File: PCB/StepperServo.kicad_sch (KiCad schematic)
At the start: 69 parts

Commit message: Clean
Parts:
- removed P1: (no value), symbol Connector_Generic:Conn_01x02
- removed P5: (no value), symbol StepperServo-rescue:Conn_01x02-Connector_Generic-BTTS57Bv2-rescue
- added P3: Conn_01x04, Connector_JST:JST_XH_B4B-XH-A_1x04_P2.50mm_Vertical, symbol StepperServo-rescue:Conn_01x04-Connector_Generic-BTTS57Bv2-rescue
- C1, C10: value (none) -> 100uF 35V VT; footprint (none) -> Capacitor_SMD:CP_Elec_6.3x7.7
- C11, C12, C13, C14, C16, C18, C2, C20, C21, C4, C5, C8: value (none) -> C; footprint (none) -> Capacitor_SMD:C_0603_1608Metric
- C15, C3: value (none) -> 0.22uF; footprint (none) -> Capacitor_SMD:C_0805_2012Metric
- C17, C6, C7, C9: value (none) -> C; footprint (none) -> Capacitor_SMD:C_0805_2012Metric
- C19: value (none) -> 100nF; footprint (none) -> Capacitor_SMD:C_0603_1608Metric
- D1, D4: value (none) -> LED; footprint (none) -> LED_SMD:LED_0603_1608Metric
- D2, D3, D5: value (none) -> D; footprint (none) -> Diode_SMD:D_2512_6332Metric
- H1, H2, H3, H4, H5, H6, H7, H8: value (none) -> MountingHole_Pad; footprint (none) -> MountingHole:MountingHole_2.7mm_M2.5_ISO14580_Pad_TopBottom
- L1: value (none) -> 22uH; footprint (none) -> Inductor_SMD:L_Wuerth_MAPI-4030
- Mode-K3, Next-K2, RES-K1, Valid-K4: value (none) -> SW_Push; footprint (none) -> Button_Switch_SMD:SW_SPST_TL3342
- P2: value (none) -> Conn_01x04; footprint (none) -> Connector_JST:JST_XH_B4B-XH-A_1x04_P2.50mm_Vertical
- P4: value (none) -> Conn_01x08; footprint (none) -> Connector_PinHeader_2.54mm:PinHeader_1x08_P2.54mm_Vertical
- R1, R2: value (none) -> 0.1R; footprint (none) -> Resistor_SMD:R_2512_6332Metric
- R10, R11, R13, R14, R16, R17, R21, R23, R7: value (none) -> ?R; footprint (none) -> Resistor_SMD:R_0603_1608Metric
- R18: value (none) -> 470; footprint (none) -> Resistor_SMD:R_0805_2012Metric
- R19: value (none) -> ?R; footprint (none) -> Resistor_SMD:R_1206_3216Metric
- R20, R93: value (none) -> 1kR; footprint (none) -> Resistor_SMD:R_0603_1608Metric
- R22: value (none) -> 10k; footprint (none) -> Resistor_SMD:R_0603_1608Metric
- R6: value (none) -> 1k; footprint (none) -> Resistor_SMD:R_0603_1608Metric
- U1: value (none) -> AOZ1282CI; footprint (none) -> Package_TO_SOT_SMD:SOT-23-6
- U2, U4: value (none) -> A4950E; footprint (none) -> Package_SO:SOIC-8-1EP_3.9x4.9mm_P1.27mm_EP2.41x3.3mm
- U5: value (none) -> TLE5012B; footprint (none) -> Package_SO:Infineon_PG-DSO-8-27_3.9x4.9mm_EP2.65x3mm
- U7: value (none) -> STM32F103CBTx; footprint (none) -> Package_QFP:LQFP-48_7x7mm_P0.5mm
- U8: value (none) -> LD1117S33CTR; footprint (none) -> Package_TO_SOT_SMD:SOT-223
- U9: value (none) -> PCA82C251; footprint (none) -> Package_SO:SO-8_3.9x4.9mm_P1.27mm
- Y1: value (none) -> Crystal; footprint (none) -> Crystal:Crystal_SMD_EuroQuartz_MT-4Pin_3.2x2.5mm_HandSoldering
- p7: value (none) -> Conn_01x08; footprint (none) -> Connector_PinSocket_2.54mm:PinSocket_1x07_P2.54mm_Vertical
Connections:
- net GND: now also P3.4 (Pin_4)
- net VMOT: now also P3.1 (Pin_1)
- net CAN_L: now reaches R19.1, U9.6 (CAN-)
- net CAN_H: now reaches R19.2, U9.7 (CAN+)
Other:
- note added: "10mA"
- note added: "14mA"
- note added: "42+14+10+10+5 = 81"
- note added: "42mA"
- note added: "SN65HVD231 10-17mA"
- company: (none) -> RetroPilot
- title: (none) -> StepperServoCAN

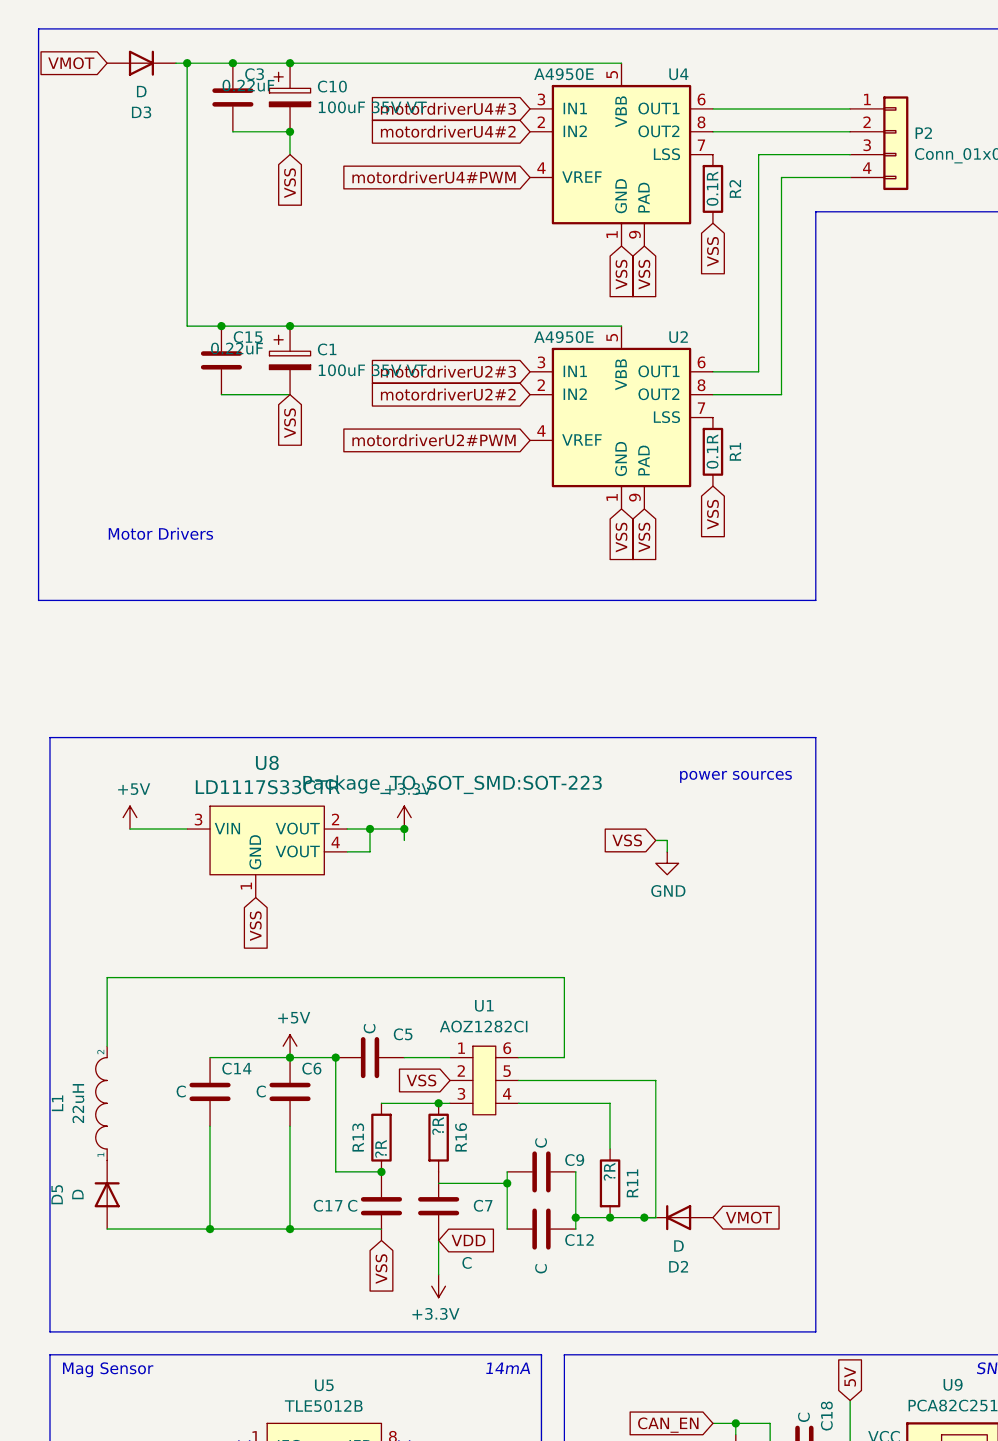
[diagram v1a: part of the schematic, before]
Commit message: S42B uses single supply diode and 5V and 3.3V lines are active when back-driving
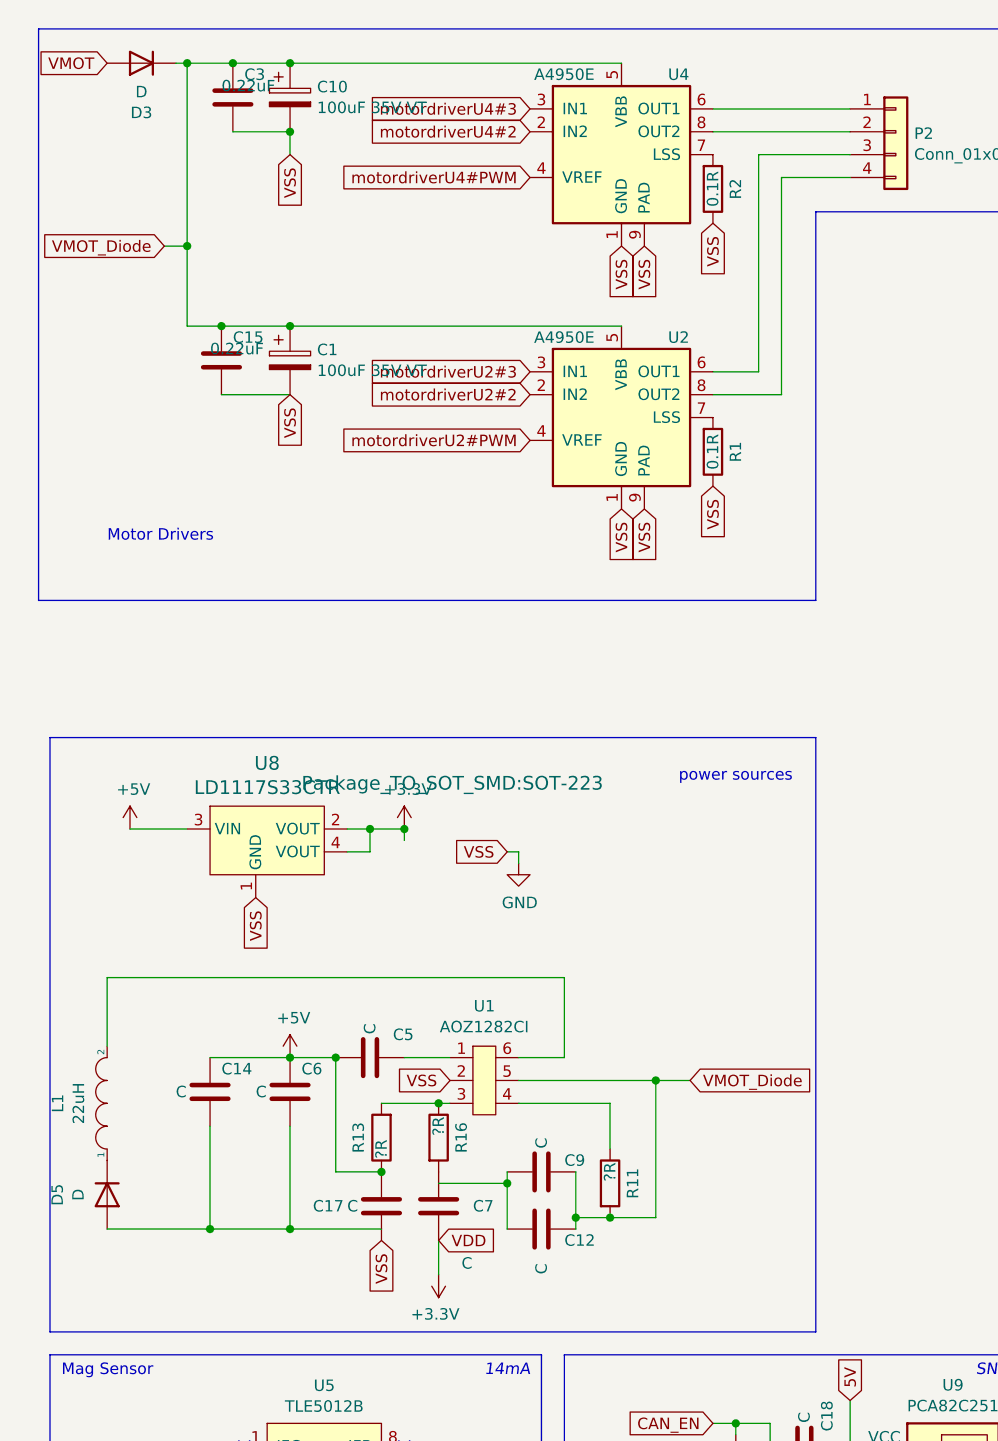
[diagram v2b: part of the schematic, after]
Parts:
- removed D2: D, Diode_SMD:D_2512_6332Metric, symbol StepperServo-rescue:D-Device-BTTS57Bv2-rescue
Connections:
- net VMOT_Diode: now reaches C1.1, C10.1, C15.1, C3.1, D3.1 (K), U2.5 (VBB), U4.5 (VBB)
- net VMOT_Diode: now also C12.1, C9.1, R11.2, U1.5
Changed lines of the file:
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@@
   (junction (at 227.33 127) (diameter 0) (color 0 0 0 0)
   )
+  (junction (at 82.55 132.08) (diameter 0) (color 0 0 0 0)
+  )
   (junction (at 265.43 46.99) (diameter 0) (color 0 0 0 0)
   )
@@
   (junction (at 265.43 54.61) (diameter 0) (color 0 0 0 0)
   )
+  (junction (at 30.48 39.37) (diameter 0) (color 0 0 0 0)
+  )
   (junction (at 50.8 104.14) (diameter 0) (color 0 0 0 0)
   )
@@
   )
   (junction (at 41.91 19.05) (diameter 0) (color 0 0 0 0)
-  )
-  (junction (at 81.28 147.32) (diameter 0) (color 0 0 0 0)
   )
   (junction (at 248.92 46.99) (diameter 0) (color 0 0 0 0)
@@
     (stroke (width 0) (type default) (color 0 0 0 0))
   )
-  (wire (pts (xy 82.55 147.32) (xy 81.28 147.32))
-    (stroke (width 0) (type default) (color 0 0 0 0))
-  )
   (wire (pts (xy 275.59 54.61) (xy 265.43 54.61))
     (stroke (width 0) (type default) (color 0 0 0 0))
@@
     (stroke (width 0) (type default) (color 0 0 0 0))
   )
-  (wire (pts (xy 30.48 19.05) (xy 30.48 48.26))
+  (wire (pts (xy 30.48 19.05) (xy 30.48 39.37))
     (stroke (width 0) (type default) (color 0 0 0 0))
   )
@@
     (stroke (width 0) (type default) (color 0 0 0 0))
   )
+  (wire (pts (xy 27.94 39.37) (xy 30.48 39.37))
+    (stroke (width 0) (type default) (color 0 0 0 0))
+  )
   (wire (pts (xy 81.28 184.15) (xy 83.82 184.15))
     (stroke (width 0) (type default) (color 0 0 0 0))
@@
     (stroke (width 0) (type default) (color 0 0 0 0))
   )
+  (wire (pts (xy 30.48 39.37) (xy 30.48 48.26))
+    (stroke (width 0) (type default) (color 0 0 0 0))
+  )
   (wire (pts (xy 125.73 180.34) (xy 125.73 182.88))
     (stroke (width 0) (type default) (color 0 0 0 0))
@@
     (stroke (width 0) (type default) (color 0 0 0 0))
   )
+  (wire (pts (xy 82.55 132.08) (xy 86.36 132.08))
+    (stroke (width 0) (type default) (color 0 0 0 0))
+  )
   (wire (pts (xy 67.31 132.08) (xy 82.55 132.08))
     (stroke (width 0) (type default) (color 0 0 0 0))
   )
-  (wire (pts (xy 77.47 147.32) (xy 81.28 147.32))
+  (wire (pts (xy 77.47 147.32) (xy 82.55 147.32))
     (stroke (width 0) (type default) (color 0 0 0 0))
   )
@@
     (stroke (width 0) (type default) (color 0 0 0 0))
   )
-  (wire (pts (xy 82.55 105.41) (xy 83.82 105.41))
+  (wire (pts (xy 66.04 106.68) (xy 67.31 106.68))
     (stroke (width 0) (type default) (color 0 0 0 0))
   )
@@
     (stroke (width 0) (type default) (color 0 0 0 0))
   )
-  (wire (pts (xy 83.82 105.41) (xy 83.82 106.68))
+  (wire (pts (xy 67.31 106.68) (xy 67.31 107.95))
     (stroke (width 0) (type default) (color 0 0 0 0))
   )
@@
     )
   )
-  (global_label "VSS" (shape input) (at 82.55 105.41 180) (fields_autoplaced)
-    (effects (font (size 1.27 1.27)) (justify right))
-    (property "Intersheet References" "${INTERSHEET_REFS}" (id 0) (at 0 0 0)
+  (global_label "VSS" (shape input) (at 66.04 106.68 180) (fields_autoplaced)
+    (effects (font (size 1.27 1.27)) (justify right))
+    (property "Intersheet References" "${INTERSHEET_REFS}" (id 0) (at -16.51 1.27 0)
       (effects (font (size 1.27 1.27)) hide)
     )
@@
     )
   )
+  (global_label "VMOT_Diode" (shape input) (at 86.36 132.08 0) (fields_autoplaced)
+    (effects (font (size 1.27 1.27)) (justify left))
+    (property "Intersheet References" "${INTERSHEET_REFS}" (id 0) (at 99.7513 132.1594 0)
+      (effects (font (size 1.27 1.27)) (justify left) hide)
+    )
+  )
   (global_label "VSS" (shape input) (at 166.37 53.34 180) (fields_autoplaced)
     (effects (font (size 1.27 1.27)) (justify right))
@@
   (global_label "motordriverU2#3" (shape input) (at 68.58 53.34 180) (fields_autoplaced)
     (effects (font (size 1.27 1.27)) (justify right))
-    (property "Intersheet References" "${INTERSHEET_REFS}" (id 0) (at 0 0 0)
-      (effects (font (size 1.27 1.27)) hide)
-    )
-  )
-  (global_label "VMOT" (shape input) (at 88.9 147.32 0) (fields_autoplaced)
-    (effects (font (size 1.27 1.27)) (justify left))
     (property "Intersheet References" "${INTERSHEET_REFS}" (id 0) (at 0 0 0)
       (effects (font (size 1.27 1.27)) hide)
@@
     (property "Intersheet References" "${INTERSHEET_REFS}" (id 0) (at 0 0 0)
       (effects (font (size 1.27 1.27)) hide)
+    )
+  )
+  (global_label "VMOT_Diode" (shape input) (at 27.94 39.37 180) (fields_autoplaced)
+    (effects (font (size 1.27 1.27)) (justify right))
+    (property "Intersheet References" "${INTERSHEET_REFS}" (id 0) (at 14.5487 39.2906 0)
+      (effects (font (size 1.27 1.27)) (justify right) hide)
     )
   )
@@
     (pin "1")
   )
-  (symbol (lib_id "StepperServo-rescue:D-Device-BTTS57Bv2-rescue") (at 85.09 147.32 0) (unit 1)
-    (in_bom yes) (on_board yes)
-    (property "Reference" "D2" (id 0) (at 85.09 152.8318 0))
-    (property "Value" "D" (id 1) (at 85.09 150.5204 0))
-    (property "Footprint" "Diode_SMD:D_2512_6332Metric" (id 2) (at 85.09 147.32 0)
-      (effects (font (size 1.27 1.27)) hide)
-    )
-    (property "Datasheet" "~" (id 3) (at 85.09 147.32 0)
-      (effects (font (size 1.27 1.27)) hide)
-    )
-    (pin "1")
-    (pin "2")
-  )
   (symbol (lib_id "StepperServo-rescue:R-Device-BTTS57Bv2-rescue") (at 190.5 91.44 90) (unit 1)
     (in_bom yes) (on_board yes)
@@
     (pin "1")
   )
-  (symbol (lib_id "StepperServo-rescue:GND-power-BTTS57Bv2-rescue") (at 83.82 106.68 0) (unit 1)
-    (in_bom yes) (on_board yes)
-    (property "Reference" "#PWR0111" (id 0) (at 83.82 113.03 0)
-      (effects (font (size 1.27 1.27)) hide)
-    )
-    (property "Value" "GND" (id 1) (at 83.947 111.0742 0))
-    (property "Footprint" "" (id 2) (at 83.82 106.68 0)
-      (effects (font (size 1.27 1.27)) hide)
-    )
-    (property "Datasheet" "" (id 3) (at 83.82 106.68 0)
+  (symbol (lib_id "StepperServo-rescue:GND-power-BTTS57Bv2-rescue") (at 67.31 107.95 0) (unit 1)
+    (in_bom yes) (on_board yes)
+    (property "Reference" "#PWR0111" (id 0) (at 67.31 114.3 0)
+      (effects (font (size 1.27 1.27)) hide)
+    )
+    (property "Value" "GND" (id 1) (at 67.437 112.3442 0))
+    (property "Footprint" "" (id 2) (at 67.31 107.95 0)
+      (effects (font (size 1.27 1.27)) hide)
+    )
+    (property "Datasheet" "" (id 3) (at 67.31 107.95 0)
       (effects (font (size 1.27 1.27)) hide)
     )
@@
       (reference "D1") (unit 1) (value "LED") (footprint "LED_SMD:LED_0603_1608Metric")
     )
-    (path "/00000000-0000-0000-0000-000060b37332"
-      (reference "D2") (unit 1) (value "D") (footprint "Diode_SMD:D_2512_6332Metric")
-    )
     (path "/00000000-0000-0000-0000-000060b6c2fe"
